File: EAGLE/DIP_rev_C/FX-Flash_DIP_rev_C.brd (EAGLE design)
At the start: 50 x 69 mm, 6 parts, among them IC1 SST39SF040-70-4C-PHE, IC2 SN74LVC32ADR

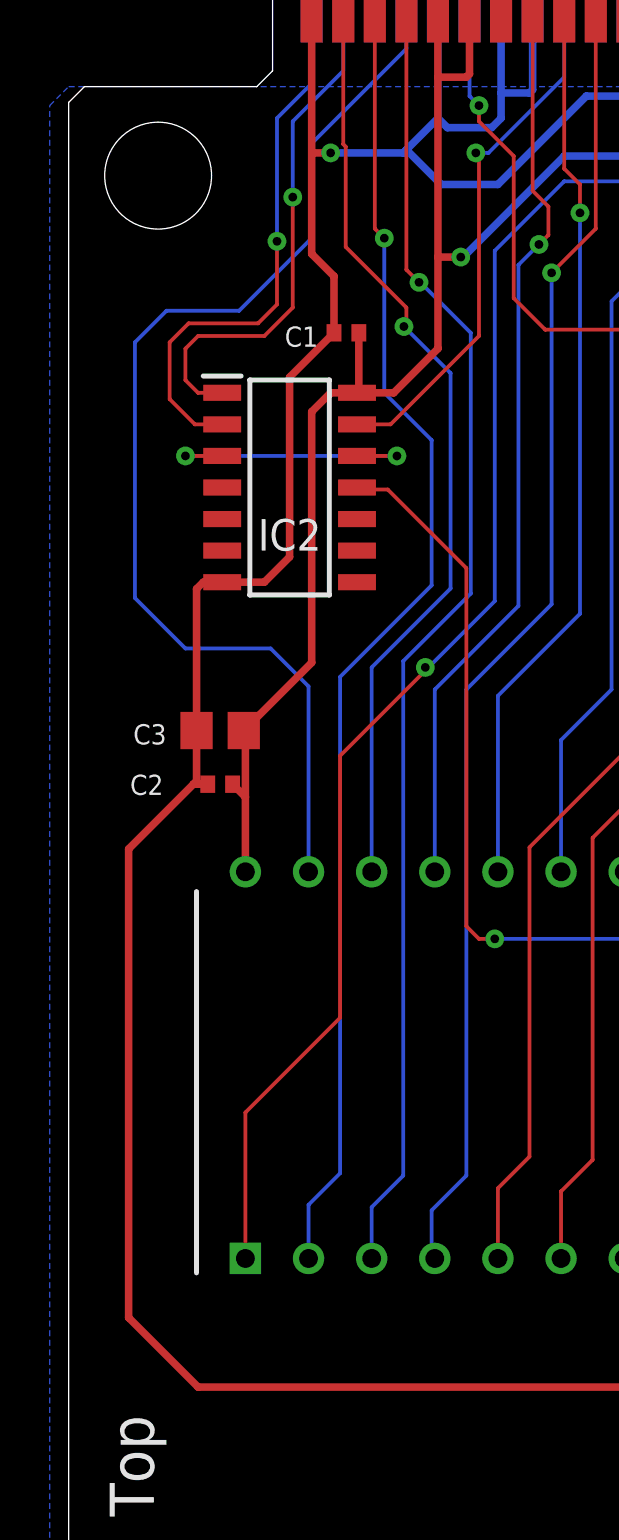
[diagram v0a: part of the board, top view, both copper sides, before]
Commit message: Update DIP design to use 0805 capacitors for easy soldering (rev C)
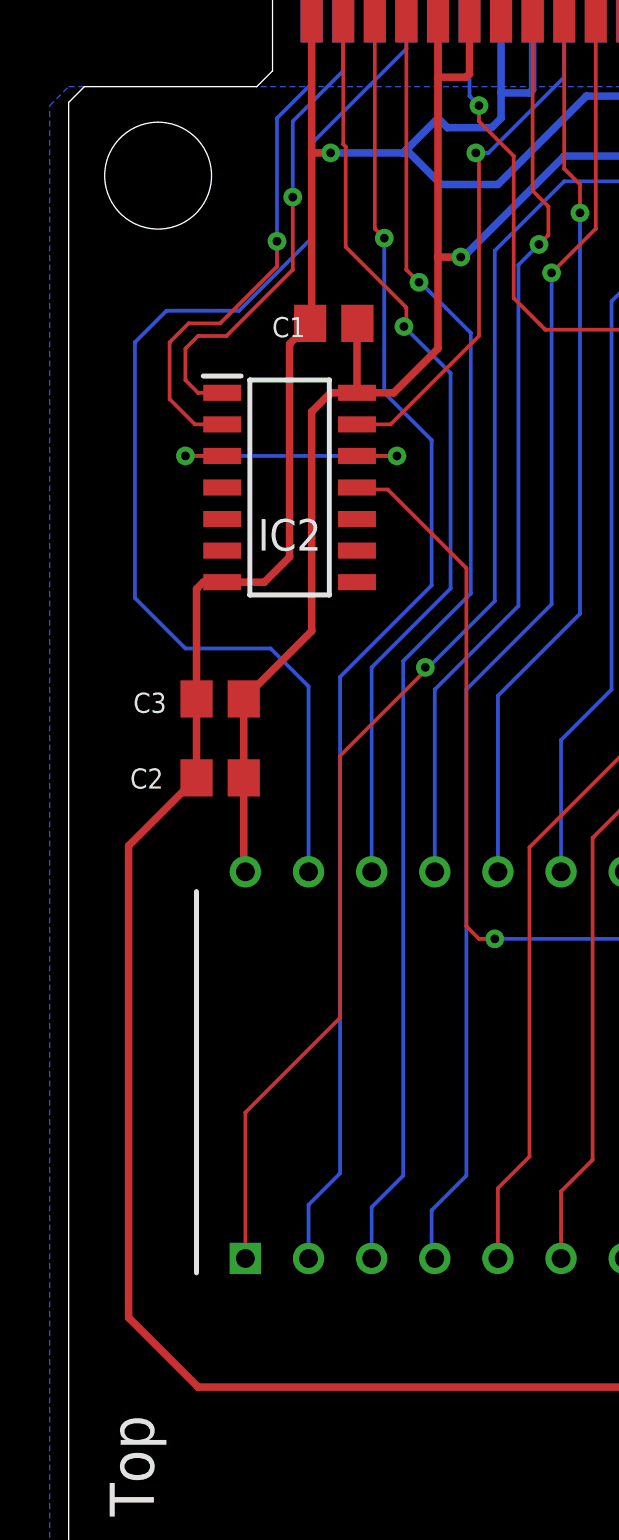
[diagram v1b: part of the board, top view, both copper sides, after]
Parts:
- C1, C2: device PC-Engine0402:C0402 -> resistor:C0805
- moved C3 1.27 mm to (6.10, 35.4)
- moved C1 0.64 mm to (10.7, 50.5)
- moved C2 0.25 mm to (6.10, 32.3)
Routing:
- net GND: track 235.6 -> 234.3 mm
- net N$22: track 23.4 -> 22.5 mm
- net N$23: track 22.0 -> 21.1 mm
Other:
- board text added: "Board Rev. C"
- board text added: "By David Shadoff (c) 2023"
- board text removed: "Board Rev. B"
- board text removed: "Prototype by David Shadoff (c) 2022"
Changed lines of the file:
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@@
 <setting verticaltext="up"/>
 </settings>
-<grid distance="5" unitdist="mil" unit="mm" style="lines" multiple="1" display="yes" altdistance="5" altunitdist="mil" altunit="mil"/>
+<grid distance="5" unitdist="mil" unit="mil" style="lines" multiple="1" display="yes" altdistance="5" altunitdist="mil" altunit="mil"/>
 <layers>
 <layer number="1" name="Top" color="4" fill="1" visible="yes" active="yes"/>
@@
 <wire x1="41.8338" y1="67.961" x2="40.8338" y2="68.961" width="0" layer="20"/>
 <wire x1="40.8338" y1="68.961" x2="9.2042" y2="68.961" width="0" layer="20"/>
-<text x="29.2862" y="1.4224" size="1.016" layer="27">Prototype by
-David Shadoff
-(c) 2022</text>
+<text x="29.2862" y="3.0734" size="1.016" layer="27">By David Shadoff
+(c) 2023</text>
 <text x="29.337" y="8.8392" size="2.1844" layer="27">FX-Flash</text>
-<text x="29.337" y="6.7564" size="1.016" layer="27">Board Rev. B</text>
+<text x="29.337" y="6.7564" size="1.016" layer="27">Board Rev. C</text>
 <text x="29.718" y="59.055" size="1.016" layer="28" rot="MR0">JLCJLCJLCJLC</text>
 <text x="40.64" y="60.198" size="0.8128" layer="27">1</text>
@@
 <attribute name="NAME" x="8.89" y="42.037" size="1.27" layer="25" align="center"/>
 </element>
-<element name="C1" library="PC-Engine0402" package="C0402" package3d_urn="urn:adsk.eagle:package:23626/2" value="100nF" x="11.176" y="50.165" smashed="yes" rot="R180">
-<attribute name="NAME" x="10.033" y="50.419" size="0.8128" layer="25" rot="R180"/>
+<element name="C1" library="resistor" library_urn="urn:adsk.eagle:library:348" package="C0805" package3d_urn="urn:adsk.eagle:package:23617/2" value="100nF" x="10.668" y="50.546" smashed="yes" rot="R180">
+<attribute name="NAME" x="9.525" y="50.8" size="0.8128" layer="25" rot="R180"/>
 </element>
-<element name="C2" library="PC-Engine0402" package="C0402" package3d_urn="urn:adsk.eagle:package:23626/2" value="100nF" x="6.096" y="32.004" smashed="yes" rot="R180">
-<attribute name="NAME" x="3.81" y="32.385" size="0.8128" layer="25" rot="R180"/>
+<element name="C2" library="resistor" library_urn="urn:adsk.eagle:library:348" package="C0805" package3d_urn="urn:adsk.eagle:package:23617/2" value="100nF" x="6.096" y="32.258" smashed="yes" rot="R180">
+<attribute name="NAME" x="3.81" y="32.639" size="0.8128" layer="25" rot="R180"/>
 </element>
 <element name="IC1" library="PC-Engine" package="DIP1556W56P254L4191H508Q32N" value="SST39SF040-70-4C-PHE" x="26.162" y="20.701" smashed="yes" rot="R90">
@@
 <attribute name="RS_PRICE-STOCK" value="http://uk.rs-online.com/web/p/products/8104037P" x="26.162" y="20.701" size="1.778" layer="27" rot="R90" display="off"/>
 </element>
-<element name="C3" library="resistor" library_urn="urn:adsk.eagle:library:348" package="C0805" package3d_urn="urn:adsk.eagle:package:23617/2" value="10uF" x="6.096" y="34.163" smashed="yes" rot="R180">
-<attribute name="NAME" x="3.937" y="34.417" size="0.8128" layer="25" rot="R180"/>
+<element name="C3" library="resistor" library_urn="urn:adsk.eagle:library:348" package="C0805" package3d_urn="urn:adsk.eagle:package:23617/2" value="10uF" x="6.096" y="35.433" smashed="yes" rot="R180">
+<attribute name="NAME" x="3.937" y="35.687" size="0.8128" layer="25" rot="R180"/>
 </element>
 </elements>
@@
 <wire x1="14.859" y1="53.213" x2="14.859" y2="60.452" width="0.3048" layer="1"/>
 <wire x1="13.081" y1="47.752" x2="14.859" y2="49.53" width="0.3048" layer="1"/>
-<wire x1="11.602" y1="47.752" x2="11.676" y2="47.826" width="0.3048" layer="1"/>
-<wire x1="11.676" y1="47.826" x2="11.676" y2="50.165" width="0.3048" layer="1"/>
 <wire x1="11.602" y1="47.752" x2="10.541" y2="47.752" width="0.3048" layer="1"/>
 <wire x1="9.779" y1="46.99" x2="10.541" y2="47.752" width="0.3048" layer="1"/>
@@
 <wire x1="27.305" y1="57.277" x2="27.305" y2="60.452" width="0.3048" layer="1"/>
 <wire x1="27.305" y1="60.452" x2="27.559" y2="60.706" width="0.3048" layer="1"/>
-<wire x1="7.112" y1="28.48" x2="7.112" y2="31.488" width="0.3048" layer="1"/>
-<wire x1="7.112" y1="31.488" x2="6.596" y2="32.004" width="0.3048" layer="1"/>
-<wire x1="7.112" y1="31.488" x2="7.112" y2="34.097" width="0.3048" layer="1"/>
-<wire x1="7.112" y1="34.097" x2="7.046" y2="34.163" width="0.3048" layer="1"/>
-<wire x1="7.046" y1="34.163" x2="9.779" y2="36.896" width="0.3048" layer="1"/>
-<wire x1="9.779" y1="36.896" x2="9.779" y2="46.99" width="0.3048" layer="1"/>
+<wire x1="9.779" y1="38.166" x2="9.779" y2="46.99" width="0.3048" layer="1"/>
+<wire x1="7.112" y1="28.48" x2="7.046" y2="28.546" width="0.3048" layer="1"/>
+<wire x1="7.046" y1="28.546" x2="7.046" y2="32.258" width="0.3048" layer="1"/>
+<wire x1="11.602" y1="47.752" x2="11.602" y2="50.53" width="0.3048" layer="1"/>
+<wire x1="11.602" y1="50.53" x2="11.618" y2="50.546" width="0.3048" layer="1"/>
+<wire x1="7.046" y1="32.258" x2="7.046" y2="35.433" width="0.3048" layer="1"/>
+<wire x1="7.046" y1="35.433" x2="9.779" y2="38.166" width="0.3048" layer="1"/>
 </signal>
 <signal name="GND">
@@
 <wire x1="6.178" y1="40.132" x2="7.874" y2="40.132" width="0.3048" layer="1"/>
 <wire x1="7.874" y1="40.132" x2="8.89" y2="41.148" width="0.3048" layer="1"/>
-<wire x1="8.89" y1="48.379" x2="10.676" y2="50.165" width="0.3048" layer="1"/>
-<wire x1="8.89" y1="41.148" x2="8.89" y2="48.379" width="0.3048" layer="1"/>
 <wire x1="9.779" y1="64.389" x2="9.779" y2="57.404" width="0.3048" layer="1"/>
-<wire x1="9.779" y1="57.404" x2="9.779" y2="53.34" width="0.3048" layer="1"/>
-<wire x1="10.676" y1="52.443" x2="10.676" y2="50.165" width="0.3048" layer="1"/>
-<wire x1="9.779" y1="53.34" x2="10.676" y2="52.443" width="0.3048" layer="1"/>
 <wire x1="17.399" y1="64.389" x2="17.399" y2="59.817" width="0.3048" layer="16"/>
 <wire x1="14.859" y1="64.389" x2="14.859" y2="58.801" width="0.3048" layer="16"/>
@@
 <wire x1="14.859" y1="58.801" x2="15.24" y2="58.42" width="0.3048" layer="16"/>
 <wire x1="45.212" y1="10.795" x2="45.212" y2="12.922" width="0.3048" layer="1"/>
-<wire x1="2.413" y1="10.541" x2="2.413" y2="29.398" width="0.3048" layer="1"/>
-<wire x1="2.413" y1="10.541" x2="5.207" y2="7.747" width="0.3048" layer="1"/>
+<wire x1="5.207" y1="7.747" x2="2.413" y2="10.541" width="0.3048" layer="1"/>
 <wire x1="5.207" y1="7.747" x2="42.164" y2="7.747" width="0.3048" layer="1"/>
 <wire x1="42.164" y1="7.747" x2="45.212" y2="10.795" width="0.3048" layer="1"/>
@@
 <vertex x="50.546" y="-0.635"/>
 </polygon>
-<wire x1="2.413" y1="29.398" x2="5.019" y2="32.004" width="0.3048" layer="1"/>
-<wire x1="5.019" y1="32.004" x2="5.596" y2="32.004" width="0.3048" layer="1"/>
-<wire x1="5.019" y1="32.004" x2="5.146" y2="32.131" width="0.3048" layer="1"/>
-<wire x1="5.146" y1="32.131" x2="5.146" y2="34.163" width="0.3048" layer="1"/>
 <wire x1="18.669" y1="59.944" x2="18.542" y2="59.817" width="0.3048" layer="16"/>
 <wire x1="18.542" y1="59.817" x2="17.399" y2="59.817" width="0.3048" layer="16"/>
 <wire x1="18.669" y1="64.389" x2="18.669" y2="59.944" width="0.3048" layer="16"/>
-<wire x1="5.146" y1="34.163" x2="5.146" y2="39.862" width="0.3048" layer="1"/>
+<wire x1="5.146" y1="35.433" x2="5.146" y2="39.862" width="0.3048" layer="1"/>
 <wire x1="5.416" y1="40.132" x2="5.146" y2="39.862" width="0.3048" layer="1"/>
 <wire x1="5.416" y1="40.132" x2="6.178" y2="40.132" width="0.3048" layer="1"/>
+<wire x1="2.413" y1="10.541" x2="2.413" y2="29.525" width="0.3048" layer="1"/>
+<wire x1="8.89" y1="49.718" x2="9.718" y2="50.546" width="0.3048" layer="1"/>
+<wire x1="8.89" y1="41.148" x2="8.89" y2="49.718" width="0.3048" layer="1"/>
+<wire x1="9.779" y1="57.404" x2="9.779" y2="50.607" width="0.3048" layer="1"/>
+<wire x1="9.779" y1="50.607" x2="9.718" y2="50.546" width="0.3048" layer="1"/>
+<wire x1="5.146" y1="35.433" x2="5.146" y2="32.258" width="0.3048" layer="1"/>
+<wire x1="2.413" y1="29.525" x2="5.146" y2="32.258" width="0.3048" layer="1"/>
 </signal>
 <signal name="N$3">
@@
 <wire x1="9.779" y1="60.198" x2="8.382" y2="58.801" width="0.1524" layer="16"/>
 <via x="8.382" y="53.848" extent="1-16" drill="0.35"/>
-<wire x1="8.382" y1="53.848" x2="8.382" y2="51.308" width="0.1524" layer="1"/>
-<wire x1="8.382" y1="51.308" x2="7.62" y2="50.546" width="0.1524" layer="1"/>
-<wire x1="7.62" y1="50.546" x2="4.826" y2="50.546" width="0.1524" layer="1"/>
+<wire x1="8.382" y1="53.848" x2="8.382" y2="52.832" width="0.1524" layer="1"/>
+<wire x1="8.382" y1="52.832" x2="6.096" y2="50.546" width="0.1524" layer="1"/>
+<wire x1="6.096" y1="50.546" x2="4.826" y2="50.546" width="0.1524" layer="1"/>
 <wire x1="4.826" y1="50.546" x2="4.064" y2="49.784" width="0.1524" layer="1"/>
 <wire x1="4.064" y1="47.498" x2="5.08" y2="46.482" width="0.1524" layer="1"/>
@@
 <wire x1="9.017" y1="58.674" x2="9.017" y2="55.626" width="0.1524" layer="16"/>
 <via x="9.017" y="55.626" extent="1-16" drill="0.35"/>
-<wire x1="9.017" y1="55.626" x2="9.017" y2="51.181" width="0.1524" layer="1"/>
-<wire x1="7.874" y1="50.038" x2="5.207" y2="50.038" width="0.1524" layer="1"/>
+<wire x1="9.017" y1="55.626" x2="9.017" y2="52.705" width="0.1524" layer="1"/>
+<wire x1="6.35" y1="50.038" x2="5.207" y2="50.038" width="0.1524" layer="1"/>
 <wire x1="5.207" y1="50.038" x2="4.699" y2="49.53" width="0.1524" layer="1"/>
 <wire x1="4.699" y1="48.26" x2="5.207" y2="47.752" width="0.1524" layer="1"/>
 <wire x1="11.049" y1="60.706" x2="9.017" y2="58.674" width="0.1524" layer="16"/>
-<wire x1="9.017" y1="51.181" x2="7.874" y2="50.038" width="0.1524" layer="1"/>
+<wire x1="9.017" y1="52.705" x2="6.35" y2="50.038" width="0.1524" layer="1"/>
 <wire x1="4.699" y1="49.53" x2="4.699" y2="48.26" width="0.1524" layer="1"/>
 </signal>
